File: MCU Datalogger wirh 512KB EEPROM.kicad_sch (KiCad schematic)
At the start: 25 parts, among them IC1 ATMEGA328P-AU, U1 24LC1025, U2 24LC1025, U3 DS1137S+, Y1 16 MHz, Y2 32.768 KHz

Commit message: Done the layout and wiring of the 2 layered PCB.
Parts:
- BT1: footprint Battery:BatteryHolder_Keystone_1042_1x18650 -> Connector_PinHeader_2.54mm:PinHeader_1x02_P2.54mm_Vertical
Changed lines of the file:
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@@
 			)
 		)
-		(property "Footprint" "Battery:BatteryHolder_Keystone_1042_1x18650"
+		(property "Footprint" "Connector_PinHeader_2.54mm:PinHeader_1x02_P2.54mm_Vertical"
 			(at 209.55 82.296 90)
 			(effects

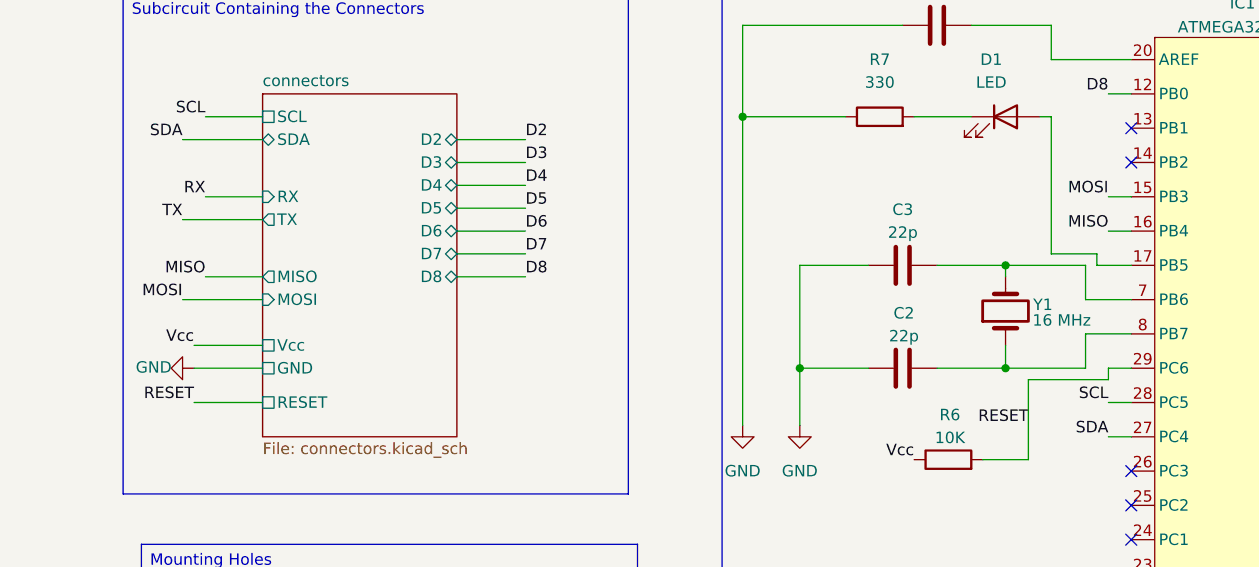
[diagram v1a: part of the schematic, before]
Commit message: Fixed the problem with the clock signal. I've added SCK for the clock signal of SPI commmunication protocol.
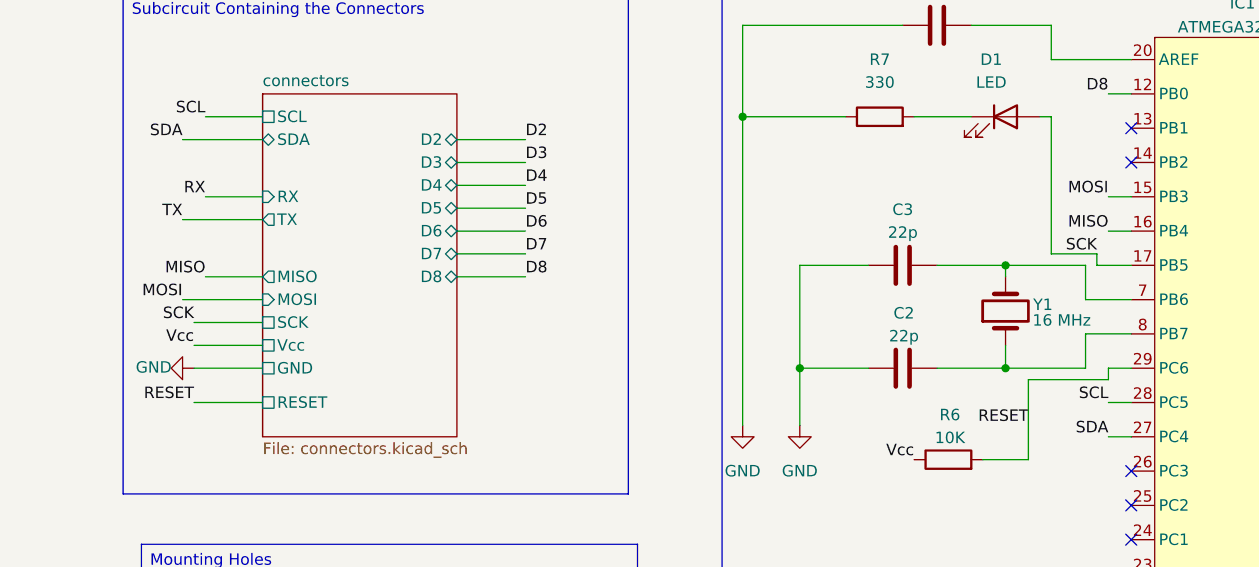
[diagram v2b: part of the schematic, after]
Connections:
- net SCK: now reaches D1.2 (A), IC1.17 (PB5)
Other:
- sheet connectors ports: added SCK; removed none
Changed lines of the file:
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@@
 	(wire
 		(pts
+			(xy 36.83 105.41) (xy 44.45 105.41)
+		)
+		(stroke
+			(width 0)
+			(type default)
+		)
+	)
+	(wire
+		(pts
 			(xy 172.72 83.82) (xy 172.72 80.01)
 		)
@@
 		)
 	)
+	(label "SCK"
+		(at 137.16 97.79 180)
+		(effects
+			(font
+				(size 1.27 1.27)
+			)
+			(justify right bottom)
+		)
+	)
 	(label "Vcc"
 		(at 92.71 25.4 0)
@@
 		)
 	)
+	(label "SCK"
+		(at 36.83 105.41 180)
+		(effects
+			(font
+				(size 1.27 1.27)
+			)
+			(justify right bottom)
+		)
+	)
 	(label "D7"
 		(at 170.18 93.98 0)
@@
 			(effects
 				(font
+					(size 1.27 1.27)
+				)
+				(justify left)
+			)
+		)
+		(pin "SCK" passive
+			(at 44.45 105.41 180)
+			(effects
+				(font
